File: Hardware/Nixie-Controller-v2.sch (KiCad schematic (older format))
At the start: 18 parts, among them U1 MAX1771, U2 NCP1117-5.0, U3 NCP1117-3.3

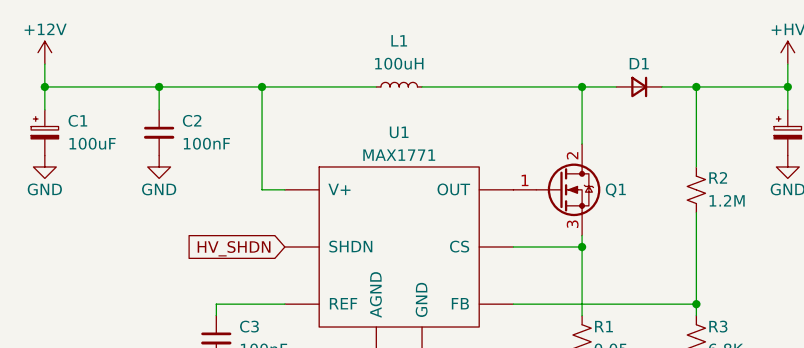
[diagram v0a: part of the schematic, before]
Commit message: Optimize power supply inductor
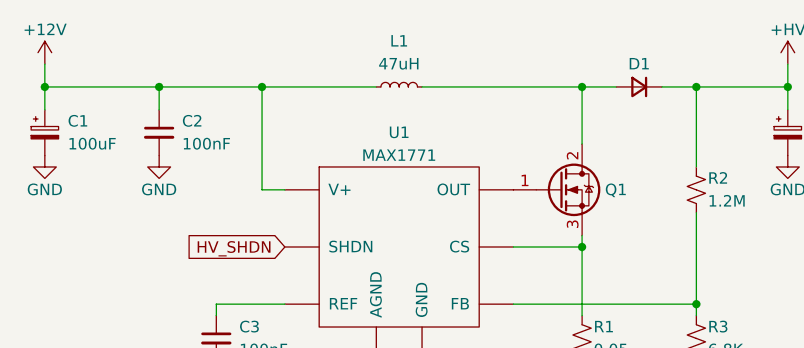
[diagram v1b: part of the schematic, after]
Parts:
- L1: value 100uH -> 47uH; Part# SRR1210A-151M -> SRR1210A-470M
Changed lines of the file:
@@
 P 2550 1050
 F 0 "L1" V 2750 1050 50  0000 C CNN
-F 1 "100uH" V 2650 1050 50  0000 C CNN
+F 1 "47uH" V 2650 1050 50  0000 C CNN
 F 2 "Inductor_SMD:L_Bourns_SRR1210A" H 2550 1050 50  0001 C CNN
 F 3 "~" H 2550 1050 50  0001 C CNN
 F 4 "Bourns" H 2550 1050 50  0001 C CNN "Manufacturer"
-F 5 "SRR1210A-151M" H 2550 1050 50  0001 C CNN "Part#"
+F 5 "SRR1210A-470M" H 2550 1050 50  0001 C CNN "Part#"
 	1    2550 1050
 	0    -1   -1   0

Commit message: Add tube driving circuitry
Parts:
- added C? (x16): 100nF, Capacitor_SMD:C_0402_1005Metric, symbol Device:C_Small
- added J? (x6): ~, symbol Connector:Conn_01x11_Female
- added Q? (x60): ~, symbol Device:Q_NPN_EBC
- added R? (x6): 470, symbol Device:R_Small_US
- added R? (x60): 6.8K, Resistor_SMD:R_0402_1005Metric, symbol Device:R_Small_US
- added U? (x3): 74HC595, symbol Nixie-Controller-v2:74HC595
- added U? (x6): 74HC4067, symbol Nixie-Controller-v2:74HC4067
- added U? (x6): OPA180, symbol Nixie-Controller-v2:OPA180
- added U?: BH2226, symbol Nixie-Controller-v2:BH2226
- added U?: SN74LVCC3245A, symbol Nixie-Controller-v2:SN74LVCC3245A
- renumbered C1 to C?, C4 to C?, C3 to C?, C2 to C?, C5 to C?, C6 to C?, C7 to C?, C8 to C?, D1 to D?, L1 to L?, Q1 to Q?, R1 to R?, R2 to R?, R3 to R?, RV1 to RV?, U1 to U?, U2 to U?, U3 to U?
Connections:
- net +3V3: now also U?.1 (VCCA), U?.2 (DIR)
- net +5V: now also C?.1, C?.1, C?.1, C?.1, C?.1, C?.1, C?.1, C?.1, C?.1, C?.1, C?.1, C?.1, C?.1, C?.1, C?.1, C?.1, U?.10 (~RST), U?.10 (~RST), U?.10 (~RST), U?.10 (~RST), U?.16 (VCC), U?.16 (VCC), U?.16 (VCC), U?.24 (VCC), U?.24 (VCC), U?.24 (VCC), U?.24 (VCC), U?.24 (VCC), U?.24 (VCC), U?.24 (VCCB), U?.5 (V+), U?.5 (V+), U?.5 (V+), U?.5 (V+), U?.5 (V+), U?.5 (V+), U?.9 (VCC)
- net +HV: now also J?.1 (Pin_1), J?.1 (Pin_1), J?.1 (Pin_1), J?.1 (Pin_1), J?.1 (Pin_1), J?.1 (Pin_1)
- net GND: now also C?.2, C?.2, C?.2, C?.2, C?.2, C?.2, C?.2, C?.2, C?.2, C?.2, C?.2, C?.2, C?.2, C?.2, C?.2, C?.2, R?.1, R?.1, R?.1, R?.1, R?.1, R?.1, R?.1, R?.1, R?.1, R?.1, R?.1, R?.1, R?.1, R?.1, R?.1, R?.1, R?.1, R?.1, R?.1, R?.1, R?.1, R?.1, R?.1, R?.1, R?.1, R?.1, R?.1, R?.1, R?.1, R?.1, R?.1, R?.1, R?.1, R?.1, R?.1, R?.1, R?.1, R?.1, R?.1, R?.1, R?.1, R?.1, R?.1, R?.1, R?.1, R?.1, R?.1, R?.1, R?.1, R?.1, R?.1, R?.1, R?.1, R?.1, R?.1, R?.1, R?.1, R?.1, R?.1, R?.1, R?.2, R?.2, R?.2, R?.2, R?.2, R?.2, U?.11 (GND), U?.11 (TEST), U?.12 (GND), U?.12 (GND), U?.12 (GND), U?.12 (GND), U?.12 (GND), U?.12 (GND), U?.12 (GND), U?.13 (GND), U?.13 (~OE), U?.13 (~OE), U?.13 (~OE), U?.15 (~EN), U?.15 (~EN), U?.15 (~EN), U?.15 (~EN), U?.15 (~EN), U?.15 (~EN), U?.16 (GND), U?.2 (V-), U?.2 (V-), U?.2 (V-), U?.2 (V-), U?.2 (V-), U?.2 (V-), U?.22 (~OE), U?.8 (GND), U?.8 (GND), U?.8 (GND)
- new net: U?.14 (DATA), U?.9 (Q7S) (x2)
- new net: U?.1, U?.1 (C) (x6)
- new net: Q?.2 (B), R?.2, U?.2 (Q7) (x6)
- new net: Q?.2 (B), R?.2, U?.22 (Q9) (x6)
- new net: Q?.2 (B), R?.2, U?.23 (Q8) (x6)
- new net: Q?.2 (B), R?.2, U?.3 (Q6) (x6)
- new net: Q?.2 (B), R?.2, U?.4 (Q5) (x6)
- new net: Q?.2 (B), R?.2, U?.5 (Q4) (x6)
- new net: Q?.2 (B), R?.2, U?.6 (Q3) (x6)
- new net: Q?.2 (B), R?.2, U?.7 (Q2) (x6)
- new net: Q?.2 (B), R?.2, U?.8 (Q1) (x6)
- new net: Q?.2 (B), R?.2, U?.9 (Q0) (x6)
- new net: Q?.1 (E), Q?.1 (E), Q?.1 (E), Q?.1 (E), Q?.1 (E), Q?.1 (E), Q?.1 (E), Q?.1 (E), Q?.1 (E), Q?.1 (E), R?.1, U?.4 (-) (x6)
- new net 3V3_DAC_MOSI: U?.7 (A5)
- new net 3V3_DAC_SCK: U?.6 (A4)
- new net 3V3_DAC_nCS: U?.8 (A6)
- new net 3V3_SR_DATA: U?.3 (A1)
- new net 3V3_SR_LATCH: U?.5 (A3)
- new net 3V3_SR_SHIFT: U?.4 (A2)
- new net D0-G0: J?.2 (Pin_2), Q?.3 (C)
- new net D0-G1: J?.3 (Pin_3), Q?.3 (C)
- new net D0-G2: J?.4 (Pin_4), Q?.3 (C)
- new net D0-G3: J?.5 (Pin_5), Q?.3 (C)
- new net D0-G4: J?.6 (Pin_6), Q?.3 (C)
- new net D0-G5: J?.7 (Pin_7), Q?.3 (C)
- new net D0-G6: J?.8 (Pin_8), Q?.3 (C)
- new net D0-G7: J?.9 (Pin_9), Q?.3 (C)
- new net D0-G8: J?.10 (Pin_10), Q?.3 (C)
- new net D0-G9: J?.11 (Pin_11), Q?.3 (C)
- new net D0-S0: U?.10 (S0), U?.4 (Q4)
- new net D0-S1: U?.11 (S1), U?.5 (Q5)
- new net D0-S2: U?.14 (S2), U?.6 (Q6)
- new net D0-S3: U?.13 (S3), U?.7 (Q7)
- new net D0-VREF: U?.1 (DA1), U?.3 (+)
- new net D1-G0: J?.2 (Pin_2), Q?.3 (C)
- new net D1-G1: J?.3 (Pin_3), Q?.3 (C)
- new net D1-G2: J?.4 (Pin_4), Q?.3 (C)
- new net D1-G3: J?.5 (Pin_5), Q?.3 (C)
- new net D1-G4: J?.6 (Pin_6), Q?.3 (C)
- new net D1-G5: J?.7 (Pin_7), Q?.3 (C)
- new net D1-G6: J?.8 (Pin_8), Q?.3 (C)
- new net D1-G7: J?.9 (Pin_9), Q?.3 (C)
- new net D1-G8: J?.10 (Pin_10), Q?.3 (C)
- new net D1-G9: J?.11 (Pin_11), Q?.3 (C)
- new net D1-S0: U?.10 (S0), U?.15 (Q0)
- new net D1-S1: U?.1 (Q1), U?.11 (S1)
- new net D1-S2: U?.14 (S2), U?.2 (Q2)
- new net D1-S3: U?.13 (S3), U?.3 (Q3)
- new net D1-VREF: U?.2 (DA2), U?.3 (+)
- new net D2-G0: J?.2 (Pin_2), Q?.3 (C)
- new net D2-G1: J?.3 (Pin_3), Q?.3 (C)
- new net D2-G2: J?.4 (Pin_4), Q?.3 (C)
- new net D2-G3: J?.5 (Pin_5), Q?.3 (C)
- new net D2-G4: J?.6 (Pin_6), Q?.3 (C)
- new net D2-G5: J?.7 (Pin_7), Q?.3 (C)
- new net D2-G6: J?.8 (Pin_8), Q?.3 (C)
- new net D2-G7: J?.9 (Pin_9), Q?.3 (C)
- new net D2-G8: J?.10 (Pin_10), Q?.3 (C)
- new net D2-G9: J?.11 (Pin_11), Q?.3 (C)
- new net D2-S0: U?.10 (S0), U?.4 (Q4)
- new net D2-S1: U?.11 (S1), U?.5 (Q5)
- new net D2-S2: U?.14 (S2), U?.6 (Q6)
- new net D2-S3: U?.13 (S3), U?.7 (Q7)
- new net D2-VREF: U?.3 (+), U?.3 (DA3)
- new net D3-G0: J?.2 (Pin_2), Q?.3 (C)
- new net D3-G1: J?.3 (Pin_3), Q?.3 (C)
- new net D3-G2: J?.4 (Pin_4), Q?.3 (C)
- new net D3-G3: J?.5 (Pin_5), Q?.3 (C)
- new net D3-G4: J?.6 (Pin_6), Q?.3 (C)
- new net D3-G5: J?.7 (Pin_7), Q?.3 (C)
- new net D3-G6: J?.8 (Pin_8), Q?.3 (C)
- new net D3-G7: J?.9 (Pin_9), Q?.3 (C)
- new net D3-G8: J?.10 (Pin_10), Q?.3 (C)
- new net D3-G9: J?.11 (Pin_11), Q?.3 (C)
- new net D3-S0: U?.10 (S0), U?.15 (Q0)
- new net D3-S1: U?.1 (Q1), U?.11 (S1)
- new net D3-S2: U?.14 (S2), U?.2 (Q2)
- new net D3-S3: U?.13 (S3), U?.3 (Q3)
- new net D3-VREF: U?.3 (+), U?.4 (DA4)
- new net D4-G0: J?.2 (Pin_2), Q?.3 (C)
- new net D4-G1: J?.3 (Pin_3), Q?.3 (C)
- new net D4-G2: J?.4 (Pin_4), Q?.3 (C)
- new net D4-G3: J?.5 (Pin_5), Q?.3 (C)
- new net D4-G4: J?.6 (Pin_6), Q?.3 (C)
- new net D4-G5: J?.7 (Pin_7), Q?.3 (C)
- new net D4-G6: J?.8 (Pin_8), Q?.3 (C)
- new net D4-G7: J?.9 (Pin_9), Q?.3 (C)
- new net D4-G8: J?.10 (Pin_10), Q?.3 (C)
- new net D4-G9: J?.11 (Pin_11), Q?.3 (C)
- new net D4-S0: U?.10 (S0), U?.4 (Q4)
- new net D4-S1: U?.11 (S1), U?.5 (Q5)
- new net D4-S2: U?.14 (S2), U?.6 (Q6)
- new net D4-S3: U?.13 (S3), U?.7 (Q7)
- new net D4-VREF: U?.3 (+), U?.5 (DA5)
- new net D5-G0: J?.2 (Pin_2), Q?.3 (C)
- new net D5-G1: J?.3 (Pin_3), Q?.3 (C)
- new net D5-G2: J?.4 (Pin_4), Q?.3 (C)
- new net D5-G3: J?.5 (Pin_5), Q?.3 (C)
- new net D5-G4: J?.6 (Pin_6), Q?.3 (C)
- new net D5-G5: J?.7 (Pin_7), Q?.3 (C)
- new net D5-G6: J?.8 (Pin_8), Q?.3 (C)
- new net D5-G7: J?.9 (Pin_9), Q?.3 (C)
- new net D5-G8: J?.10 (Pin_10), Q?.3 (C)
- new net D5-G9: J?.11 (Pin_11), Q?.3 (C)
- new net D5-S0: U?.10 (S0), U?.15 (Q0)
- new net D5-S1: U?.1 (Q1), U?.11 (S1)
- new net D5-S2: U?.14 (S2), U?.2 (Q2)
- new net D5-S3: U?.13 (S3), U?.3 (Q3)
- new net D5-VREF: U?.3 (+), U?.6 (DA6)
- new net DAC_MOSI: U?.14 (SI), U?.17 (B5)
- new net DAC_SCK: U?.13 (SCK), U?.18 (B4)
- new net DAC_nCS: U?.12 (~CS), U?.16 (B6)
- new net SR_DATA: U?.14 (DATA), U?.21 (B1)
- new net SR_LATCH: U?.12 (LATCH), U?.12 (LATCH), U?.12 (LATCH), U?.19 (B3)
- new net SR_SHIFT: U?.11 (SHIFT), U?.11 (SHIFT), U?.11 (SHIFT), U?.20 (B2)
- no-connect marks 1 -> 45
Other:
- note added: "CONNECTORS"
- note added: "CURRENT CONTROL DAC"
- note added: "D0: Least Significant Clock Digit\nS0: Least Significant Address Bit\n\nWhen shifting, LSDFIRST, MSBFIRST"
- note added: "DIGIT 0 FEEDBACK CONTROL"
- note added: "DIGIT 1 FEEDBACK CONTROL"
- note added: "DIGIT 2 FEEDBACK CONTROL"
- note added: "DIGIT 3 FEEDBACK CONTROL"
- note added: "DIGIT 4 FEEDBACK CONTROL"
- note added: "DIGIT 5 FEEDBACK CONTROL"
- note added: "DIGIT CONTROL"
- note added: "LEVEL SHIFTER"
- note added: "POWER"
- moved on the sheet: C?, D?, L?, Q?, R?, RV?, U?

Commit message: Add uC and component selection
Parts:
- added C? (x2): 10pF, Capacitor_SMD:C_0402_1005Metric, symbol Device:C_Small
- added C? (x5): 100nF, Capacitor_SMD:C_0402_1005Metric, symbol Device:C_Small
- added C?: 4.7uF, Capacitor_SMD:C_0603_1608Metric, symbol Device:C_Small
- added D?: LED, Diode_SMD:D_0603_1608Metric, symbol Device:LED
- added R?: 100, Resistor_SMD:R_0402_1005Metric, symbol Device:R_Small_US
- added TP? (x9): ~, symbol Connector:TestPoint
- added U?: STM32F103C8, Package_QFP:LQFP-48_7x7mm_P0.5mm, symbol Nixie-Controller-v2:STM32F103C8
- added Y?: 16MHz, Crystal:Crystal_SMD_2016-4Pin_2.0x1.6mm, symbol Device:Crystal_GND24
- C? (x18): Part# CC0402KRX5R9BB104 -> CC0402KRX7R8BB104
- J? (x6): footprint (none) -> Connector_PinSocket_2.54mm:PinSocket_1x11_P2.54mm_Vertical
- Q? (x60): footprint (none) -> Package_TO_SOT_SMD:SOT-23; Manufacturer (none) -> Nexperia; Part# (none) -> MMBTA42
- R?: Part# PE2010FKE7W0R05Z -> PE2010FKE070R05L
- R?: footprint Resistor_SMD:R_0402_1005Metric -> Resistor_SMD:R_0805_2012Metric; Part# AC0402FR-071M2L -> RC0805FR-071M2L
- R? (x61): Part# AC0402FR-076K8L -> RC0402FR-076K8L
- R? (x6): footprint (none) -> Resistor_SMD:R_0402_1005Metric; Manufacturer (none) -> Yageo; Part# (none) -> RC0402FR-07470RL
- U? (x3): footprint (none) -> Package_SO:SOIC-16_3.9x9.9mm_P1.27mm; Manufacturer (none) -> TI; Part# (none) -> CD74HC595M
- U? (x6): footprint (none) -> Package_SO:SOIC-24W_7.5x15.4mm_P1.27mm; Manufacturer (none) -> TI; Part# (none) -> CD74HC4067M
- U? (x6): footprint (none) -> Package_TO_SOT_SMD:SOT-23-5; Manufacturer (none) -> TI; Part# (none) -> OPA180IDBVT
- U?: footprint (none) -> Package_SO:SOIC-16_4.55x10.3mm_P1.27mm; Manufacturer (none) -> Rohm Semi; Part# (none) -> BH2226F-E2
- U?: footprint (none) -> Package_SO:SO-24_5.3x15mm_P1.27mm; Manufacturer (none) -> TI; Part# (none) -> SN74LVCC3245ANSR
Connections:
- net +3V3: now also C?.1, C?.1, C?.1, C?.1, C?.1, C?.1, TP?.1, U?.1 (VBAT), U?.24 (VDD), U?.36 (VDD), U?.48 (VDD), U?.9 (VDDA)
- net 3V3_DAC_MOSI: now also U?.17 (PA7)
- net 3V3_DAC_SCK: now also U?.15 (PA5)
- net 3V3_DAC_nCS: now also U?.14 (PA4)
- net 3V3_SR_DATA: now also U?.20 (PB2)
- net 3V3_SR_LATCH: now also U?.18 (PB0)
- net 3V3_SR_SHIFT: now also U?.19 (PB1)
- net GND: now also C?.1, C?.2, C?.2, C?.2, C?.2, C?.2, C?.2, C?.2, R?.1, TP?.1, TP?.1, TP?.1, U?.23 (VSS), U?.35 (VSS), U?.44 (BOOT0), U?.47 (VSS), U?.8 (VSSA), Y?.2, Y?.4
- net HV_SHDN: now also U?.21 (PB10)
- new net: D?.2 (A), U?.22 (PB11)
- new net: C?.2, U?.5 (PD0), Y?.1
- new net: C?.1, U?.6 (PD1), Y?.3
- new net: D?.1 (K), R?.2
- new net MCU_JTCLK: TP?.1, U?.37 (PA14)
- new net MCU_JTDI: TP?.1, U?.38 (PA15)
- new net MCU_JTDO: TP?.1, U?.39 (PB3)
- new net MCU_JTMS: TP?.1, U?.34 (PA13)
- new net MCU_nRST: TP?.1, U?.7 (~RST)
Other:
- note added: "ARM 10-PIN JTAG DEBUG"
- note added: "DAUGHTER BOARD CONNECTORS"
- note added: "MICROCONTROLLER"
- moved on the sheet: J?

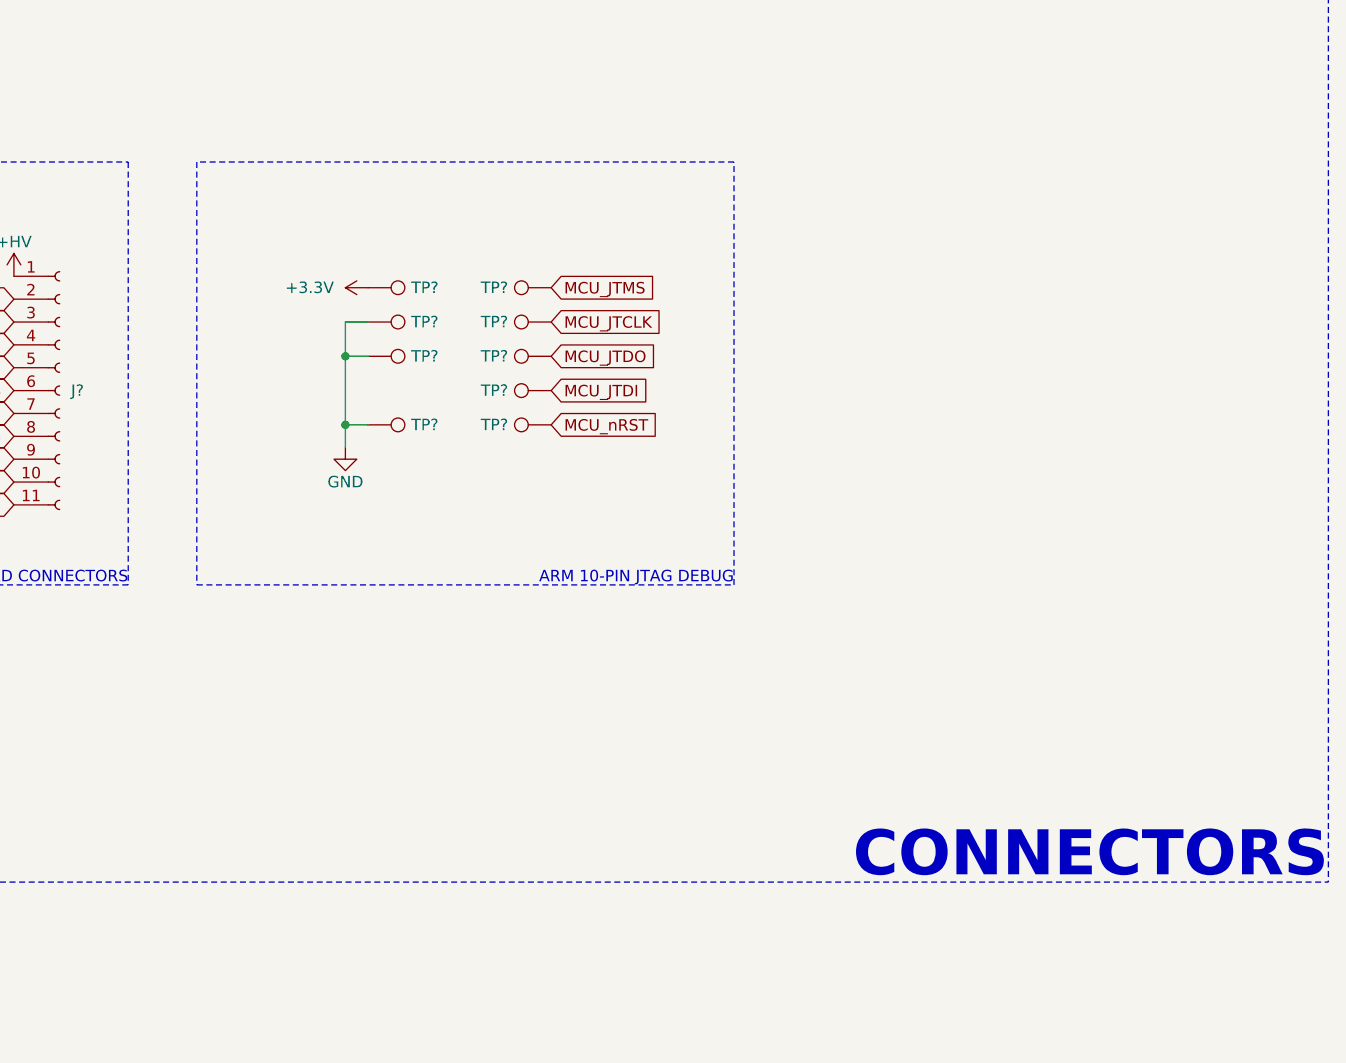
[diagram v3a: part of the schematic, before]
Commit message: Add voltage test points
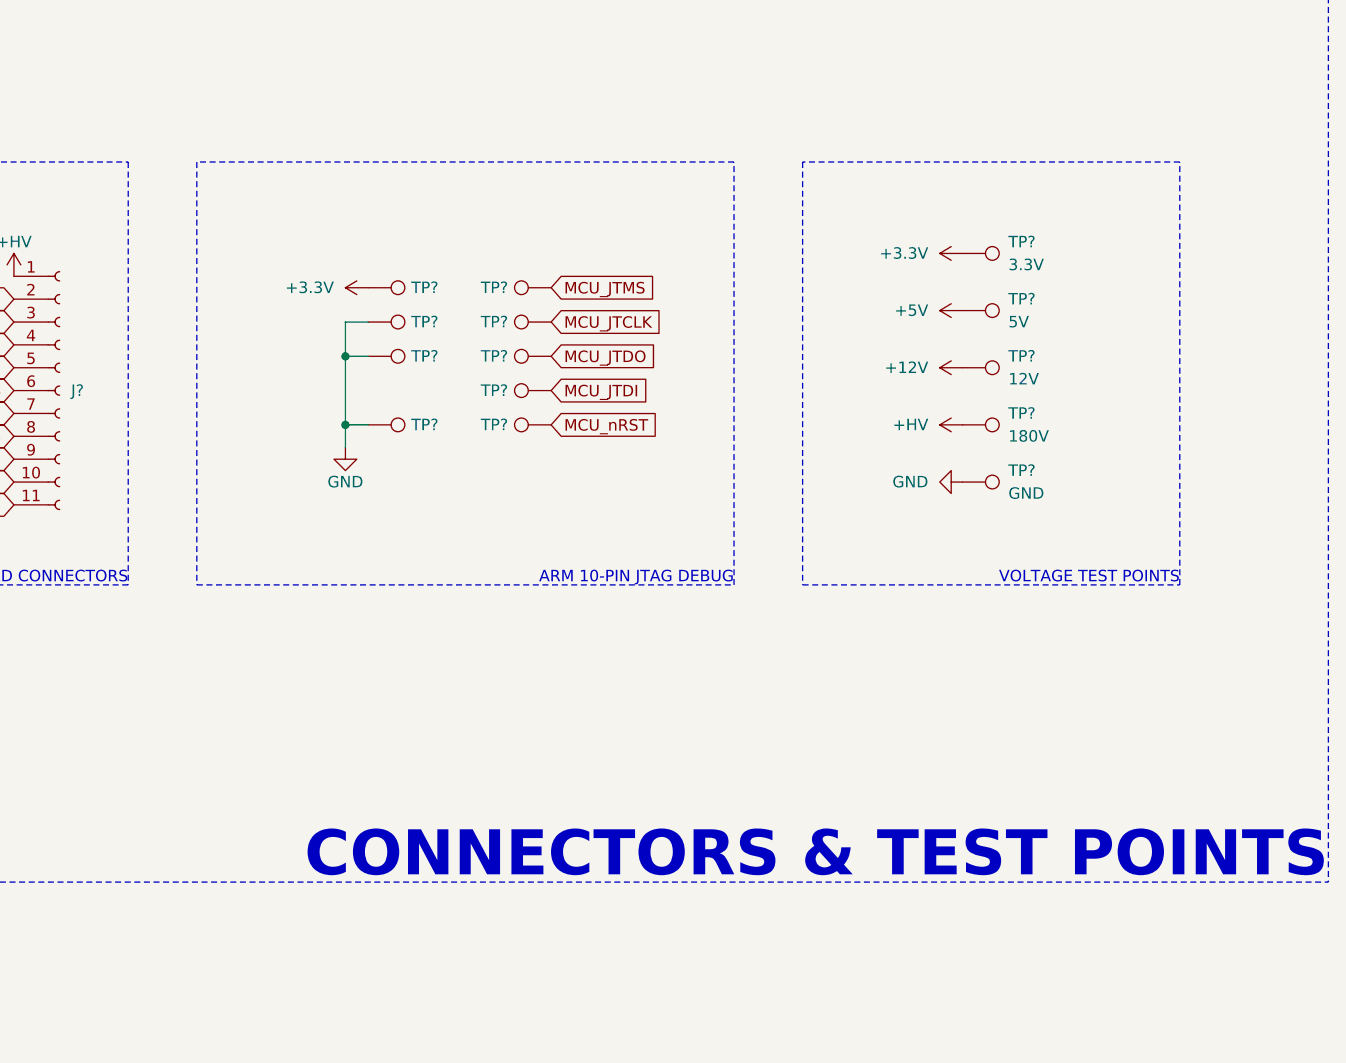
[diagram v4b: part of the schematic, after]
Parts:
- added TP?: 3.3V, symbol Connector:TestPoint
- added TP?: 5V, symbol Connector:TestPoint
- added TP?: 12V, symbol Connector:TestPoint
- added TP?: 180V, symbol Connector:TestPoint
- added TP?: GND, symbol Connector:TestPoint
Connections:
- net +12V: now also TP?.1
- net +3V3: now also TP?.1
- net +5V: now also TP?.1
- net +HV: now also TP?.1
- net GND: now also TP?.1
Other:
- note added: "CONNECTORS & TEST POINTS"
- note added: "VOLTAGE TEST POINTS"
- note removed: "CONNECTORS"
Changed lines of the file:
@@
 	32600 500  32600 5000
 Text Notes 32600 5000 2    197  ~ 39
-CONNECTORS
+CONNECTORS & TEST POINTS
 Wire Notes Line width 20
 	500  5000 32600 5000
@@
 Text Notes 30000 3700 2    50   ~ 0
 ARM 10-PIN JTAG DEBUG
+$Comp
+L Connector:TestPoint TP?
+U 1 1 61756AE0
+P 31000 2250
+F 0 "TP?" V 30950 2450 50  0000 L CNN
+F 1 "3.3V" V 31050 2450 50  0000 L CNN
+F 2 "" H 31200 2250 50  0001 C CNN
+F 3 "~" H 31200 2250 50  0001 C CNN
+	1    31000 2250
+	0    1    1    0
+$EndComp
+$Comp
+L Connector:TestPoint TP?
+U 1 1 61757D04
+P 31000 2500
+F 0 "TP?" V 30950 2700 50  0000 L CNN
+F 1 "5V" V 31050 2700 50  0000 L CNN
+F 2 "" H 31200 2500 50  0001 C CNN
+F 3 "~" H 31200 2500 50  0001 C CNN
+	1    31000 2500
+	0    1    1    0
+$EndComp
+$Comp
+L Connector:TestPoint TP?
+U 1 1 617B0935
+P 31000 2750
+F 0 "TP?" V 30950 2950 50  0000 L CNN
+F 1 "12V" V 31050 2950 50  0000 L CNN
+F 2 "" H 31200 2750 50  0001 C CNN
+F 3 "~" H 31200 2750 50  0001 C CNN
+	1    31000 2750
+	0    1    1    0
+$EndComp
+$Comp
+L Connector:TestPoint TP?
+U 1 1 618095B7
+P 31000 3000
+F 0 "TP?" V 30950 3200 50  0000 L CNN
+F 1 "180V" V 31050 3200 50  0000 L CNN
+F 2 "" H 31200 3000 50  0001 C CNN
+F 3 "~" H 31200 3000 50  0001 C CNN
+	1    31000 3000
+	0    1    1    0
+$EndComp
+$Comp
+L Connector:TestPoint TP?
+U 1 1 61862190
+P 31000 3250
+F 0 "TP?" V 30950 3450 50  0000 L CNN
+F 1 "GND" V 31050 3450 50  0000 L CNN
+F 2 "" H 31200 3250 50  0001 C CNN
+F 3 "~" H 31200 3250 50  0001 C CNN
+	1    31000 3250
+	0    1    1    0
+$EndComp
+Wire Notes Line
+	30300 1850 30300 3700
+Wire Notes Line
+	30300 3700 31950 3700
+Wire Notes Line
+	31950 3700 31950 1850
+Wire Notes Line
+	31950 1850 30300 1850
+Text Notes 31950 3700 2    50   ~ 0
+VOLTAGE TEST POINTS
+$Comp
+L power:+3.3V #PWR?
+U 1 1 61ADA641
+P 31000 2250
+F 0 "#PWR?" H 31000 2100 50  0001 C CNN
+F 1 "+3.3V" V 31000 2400 50  0000 L CNN
+F 2 "" H 31000 2250 50  0001 C CNN
+F 3 "" H 31000 2250 50  0001 C CNN
+	1    31000 2250
+	0    -1   -1   0
+$EndComp
+$Comp
+L power:+5V #PWR?
+U 1 1 61AE1943
+P 31000 2500
+F 0 "#PWR?" H 31000 2350 50  0001 C CNN
+F 1 "+5V" V 31000 2650 50  0000 L CNN
+F 2 "" H 31000 2500 50  0001 C CNN
+F 3 "" H 31000 2500 50  0001 C CNN
+	1    31000 2500
+	0    -1   -1   0
+$EndComp
+$Comp
+L power:+12V #PWR?
+U 1 1 61AE2AC5
+P 31000 2750
+F 0 "#PWR?" H 31000 2600 50  0001 C CNN
+F 1 "+12V" V 31000 2900 50  0000 L CNN
+F 2 "" H 31000 2750 50  0001 C CNN
+F 3 "" H 31000 2750 50  0001 C CNN
+	1    31000 2750
+	0    -1   -1   0
+$EndComp
+$Comp
+L Nixie-Controller-v2:+HV #PWR?
+U 1 1 61AE9748
+P 31000 3000
+F 0 "#PWR?" H 31000 2850 50  0001 C CNN
+F 1 "+HV" V 31000 3150 50  0000 L CNN
+F 2 "" H 31000 3000 50  0001 C CNN
+F 3 "" H 31000 3000 50  0001 C CNN
+	1    31000 3000
+	0    -1   -1   0
+$EndComp
+$Comp
+L power:GND #PWR?
+U 1 1 61AEC6A0
+P 31000 3250
+F 0 "#PWR?" H 31000 3000 50  0001 C CNN
+F 1 "GND" V 31000 3100 50  0000 R CNN
+F 2 "" H 31000 3250 50  0001 C CNN
+F 3 "" H 31000 3250 50  0001 C CNN
+	1    31000 3250
+	0    1    1    0
+$EndComp
 $EndSCHEMATC
